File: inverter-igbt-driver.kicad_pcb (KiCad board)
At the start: 2 copper layers, 79 x 32 mm, 41 parts, among them J1 Conn_01x06, U1 NE555, U2 IXDF604SIA, U3 FOD8316, U6 Transformer_2P_2S

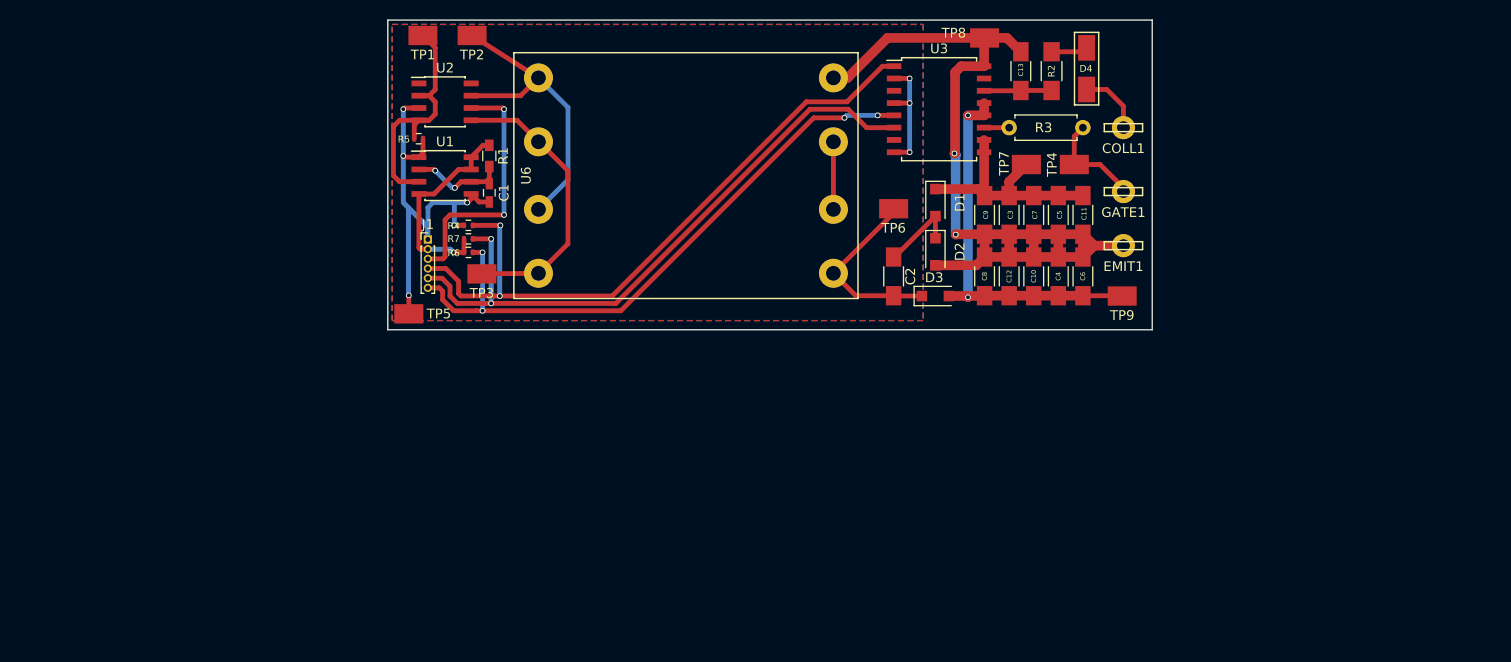
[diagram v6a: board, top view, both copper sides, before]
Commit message: Including both igbt drivers on one board.
WIP
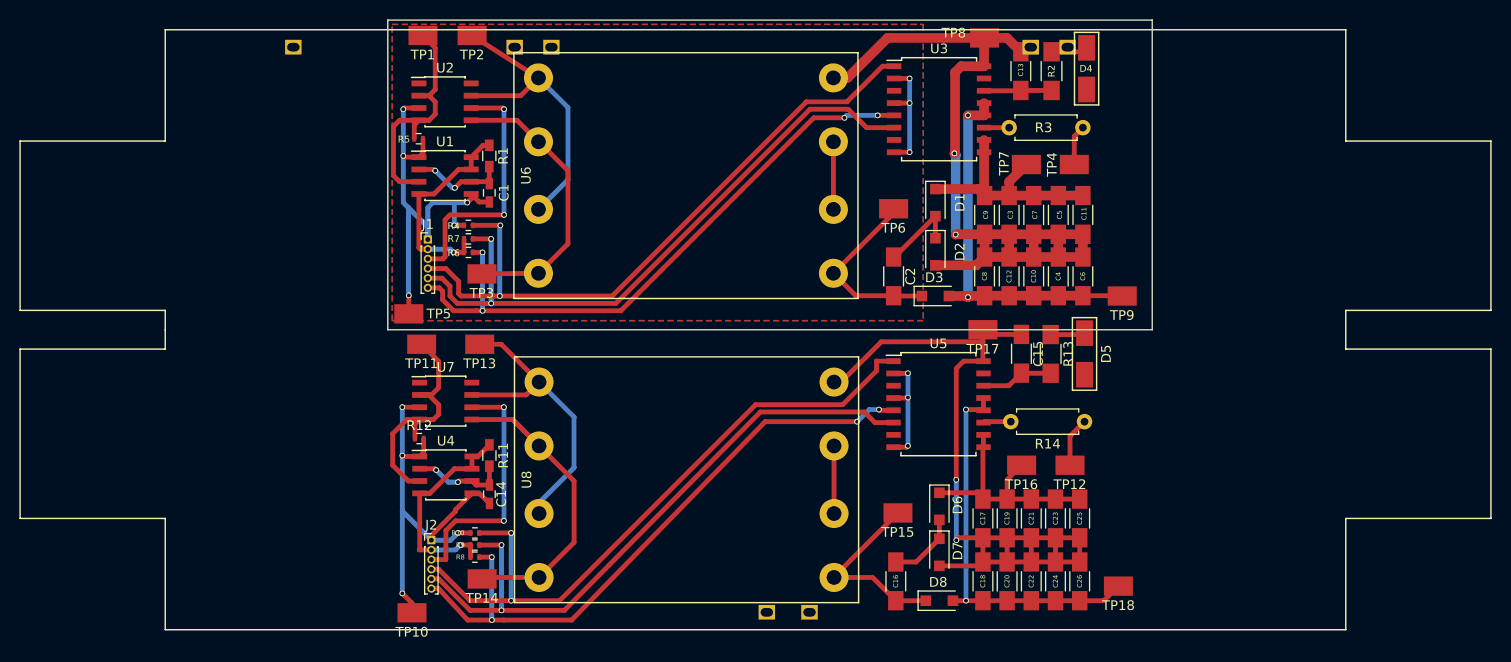
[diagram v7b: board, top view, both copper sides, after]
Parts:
- removed COLL1, EMIT1, GATE1: Conn_01x01, inverter-igbt-driver:CONN_110_TAB
- added C14: 0.01u, Capacitors_SMD:C_0603_HandSoldering, F.Cu at (110.5, 85.0)
- added C15: 100p, Capacitors_SMD:C_1206_HandSoldering, F.Cu at (165.5, 70.5)
- added C16: 10u, Capacitors_SMD:C_1206_HandSoldering, F.Cu at (152.5, 94.0)
- added C17: 10u, Capacitors_SMD:C_1206_HandSoldering, F.Cu at (161.5, 87.5)
- added C18: 10u, Capacitors_SMD:C_1206_HandSoldering, F.Cu at (161.5, 94.0)
- added C19: 10u, Capacitors_SMD:C_1206_HandSoldering, F.Cu at (164.0, 87.5)
- added C20: 10u, Capacitors_SMD:C_1206_HandSoldering, F.Cu at (164.0, 94.0)
- added C21: 10u, Capacitors_SMD:C_1206_HandSoldering, F.Cu at (166.5, 87.5)
- added C22: 10u, Capacitors_SMD:C_1206_HandSoldering, F.Cu at (166.5, 94.0)
- added C23: 10u, Capacitors_SMD:C_1206_HandSoldering, F.Cu at (169.0, 87.5)
- added C24: 10u, Capacitors_SMD:C_1206_HandSoldering, F.Cu at (169.0, 94.0)
- added C25: 10u, Capacitors_SMD:C_1206_HandSoldering, F.Cu at (171.5, 87.5)
- added C26: 10u, Capacitors_SMD:C_1206_HandSoldering, F.Cu at (171.5, 94.0)
- added D5: D, inverter-igbt-driver:DO-214AC, F.Cu at (172.0, 70.5)
- added D6: D_Schottky, Diodes_SMD:D_SOD-123F, F.Cu at (157.0, 86.2)
- added D7: D_Schottky, Diodes_SMD:D_SOD-123F, F.Cu at (157.0, 91.0)
- added D8: D_Schottky, Diodes_SMD:D_SOD-123F, F.Cu at (157.0, 96.0)
- added J2: Conn_01x06, Pin_Headers:Pin_Header_Straight_1x06_Pitch1.00mm, F.Cu at (104.5, 89.8)
- added R10: 1k, Resistors_SMD:R_0402, F.Cu at (109.0, 89.0)
- added R11: 1.5k, Resistors_SMD:R_0603_HandSoldering, F.Cu at (110.5, 81.0)
- added R12: 1k, Resistors_SMD:R_0402, F.Cu at (103.2, 79.2)
- added R13: 100, Resistors_SMD:R_1206_HandSoldering, F.Cu at (168.5, 70.5)
- added R14: 8, Resistors_THT:R_Axial_DIN0207_L6.3mm_D2.5mm_P7.62mm_Horizontal, F.Cu at (172.0, 77.5)
- added R8: 1k, Resistors_SMD:R_0402, F.Cu at (109.0, 91.5)
- added R9: 1k, Resistors_SMD:R_0402, F.Cu at (109.0, 90.2)
- added TP10: TEST, inverter-igbt-driver:TP RCT (0805), F.Cu at (102.5, 97.2)
- added TP11: TEST, inverter-igbt-driver:TP RCT (0805), F.Cu at (103.5, 69.5)
- added TP12: TEST, inverter-igbt-driver:TP RCT (0805), F.Cu at (170.5, 82.0)
- added TP13: TEST, inverter-igbt-driver:TP RCT (0805), F.Cu at (109.5, 69.5)
- added TP14: TEST, inverter-igbt-driver:TP RCT (0805), F.Cu at (109.8, 93.8)
- added TP15: TEST, inverter-igbt-driver:TP RCT (0805), F.Cu at (152.7, 86.9)
- added TP16: TEST, inverter-igbt-driver:TP RCT (0805), F.Cu at (165.5, 82.0)
- added TP17: TEST, inverter-igbt-driver:TP RCT (0805), F.Cu at (161.5, 68.0)
- added TP18: TEST, inverter-igbt-driver:TP RCT (0805), F.Cu at (175.5, 94.5)
- added U4: NE555, Housings_SOIC:SOIC-8_3.9x4.9mm_Pitch1.27mm, F.Cu at (106.0, 83.0)
- added U5: FOD8316, Housings_SOIC:SOIC-16W_7.5x10.3mm_Pitch1.27mm, F.Cu at (156.9, 75.7)
- added U7: IXDF604SIA, Housings_SOIC:SOIC-8_3.9x4.9mm_Pitch1.27mm, F.Cu at (106.0, 75.4)
- added U8: Transformer_2P_2S, inverter-igbt-driver:FS48-050-C2, F.Cu at (130.9, 83.5)
- added U9: IGBT_HALF_BRIDGE, inverter-igbt-driver:MG06600WB-BN4MM, F.Cu at (138.0, 68.0)
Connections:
- net /EMIT renamed /COLL_L
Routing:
- net /EMIT_L: track 0.00 -> 85.5 mm, vias 0 -> 2
- net /VIN_L: track 0.00 -> 70.2 mm, vias 0 -> 2
- net /FAULT_L: track 0.00 -> 67.2 mm, vias 0 -> 2
- net /RESET_L: track 0.00 -> 66.2 mm, vias 0 -> 4
- net GND: track 57.5 -> 114.3 mm, vias 8 -> 15
- net /negative/VDD_IGBT: track 0.00 -> 40.6 mm, vias 0 -> 2
- net Net-(TP14-Pad1): track 0.00 -> 34.0 mm
- net Net-(TP13-Pad1): track 0.00 -> 31.8 mm
- net +24V: track 26.4 -> 52.3 mm, vias 2 -> 4
- net /negative/VSS_IGBT: track 0.00 -> 25.5 mm
- net Net-(R12-Pad1): track 0.00 -> 25.4 mm
- net +5V: track 21.9 -> 44.6 mm, vias 1 -> 2
- net Net-(C16-Pad2): track 0.00 -> 19.9 mm
- net Net-(C14-Pad1): track 0.00 -> 9.94 mm, vias 0 -> 2
- net Net-(C15-Pad2): track 0.00 -> 7.47 mm
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
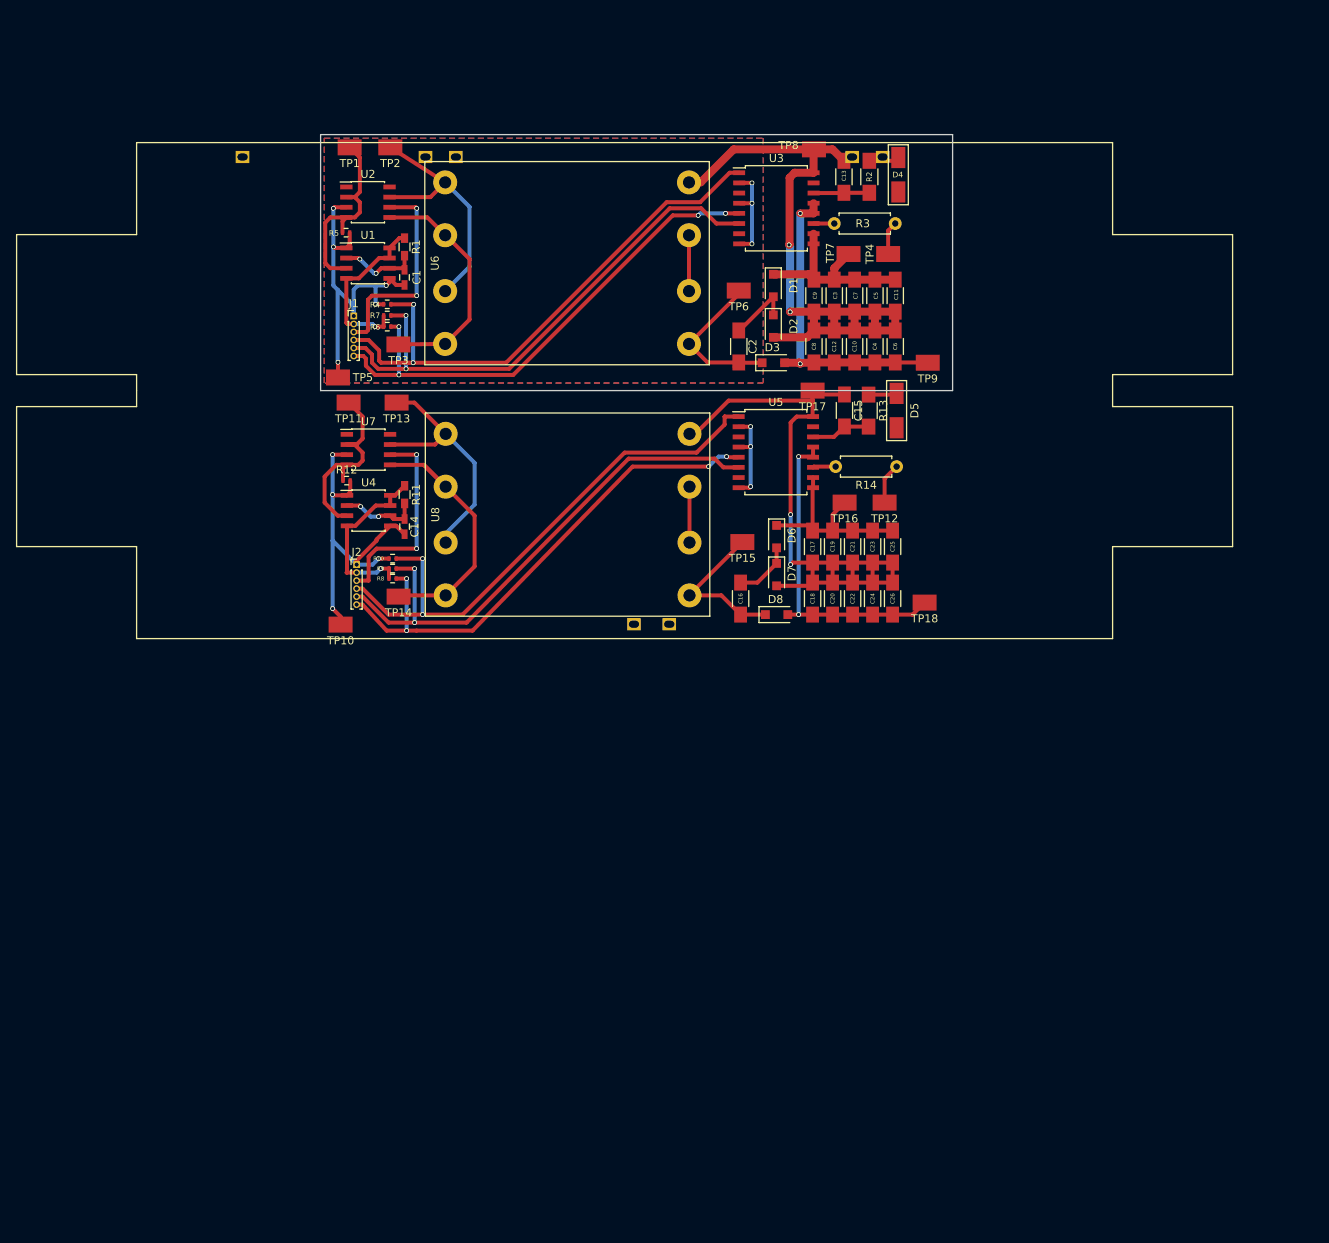
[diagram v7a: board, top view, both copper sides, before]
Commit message: Add _H suffix to hot leg.
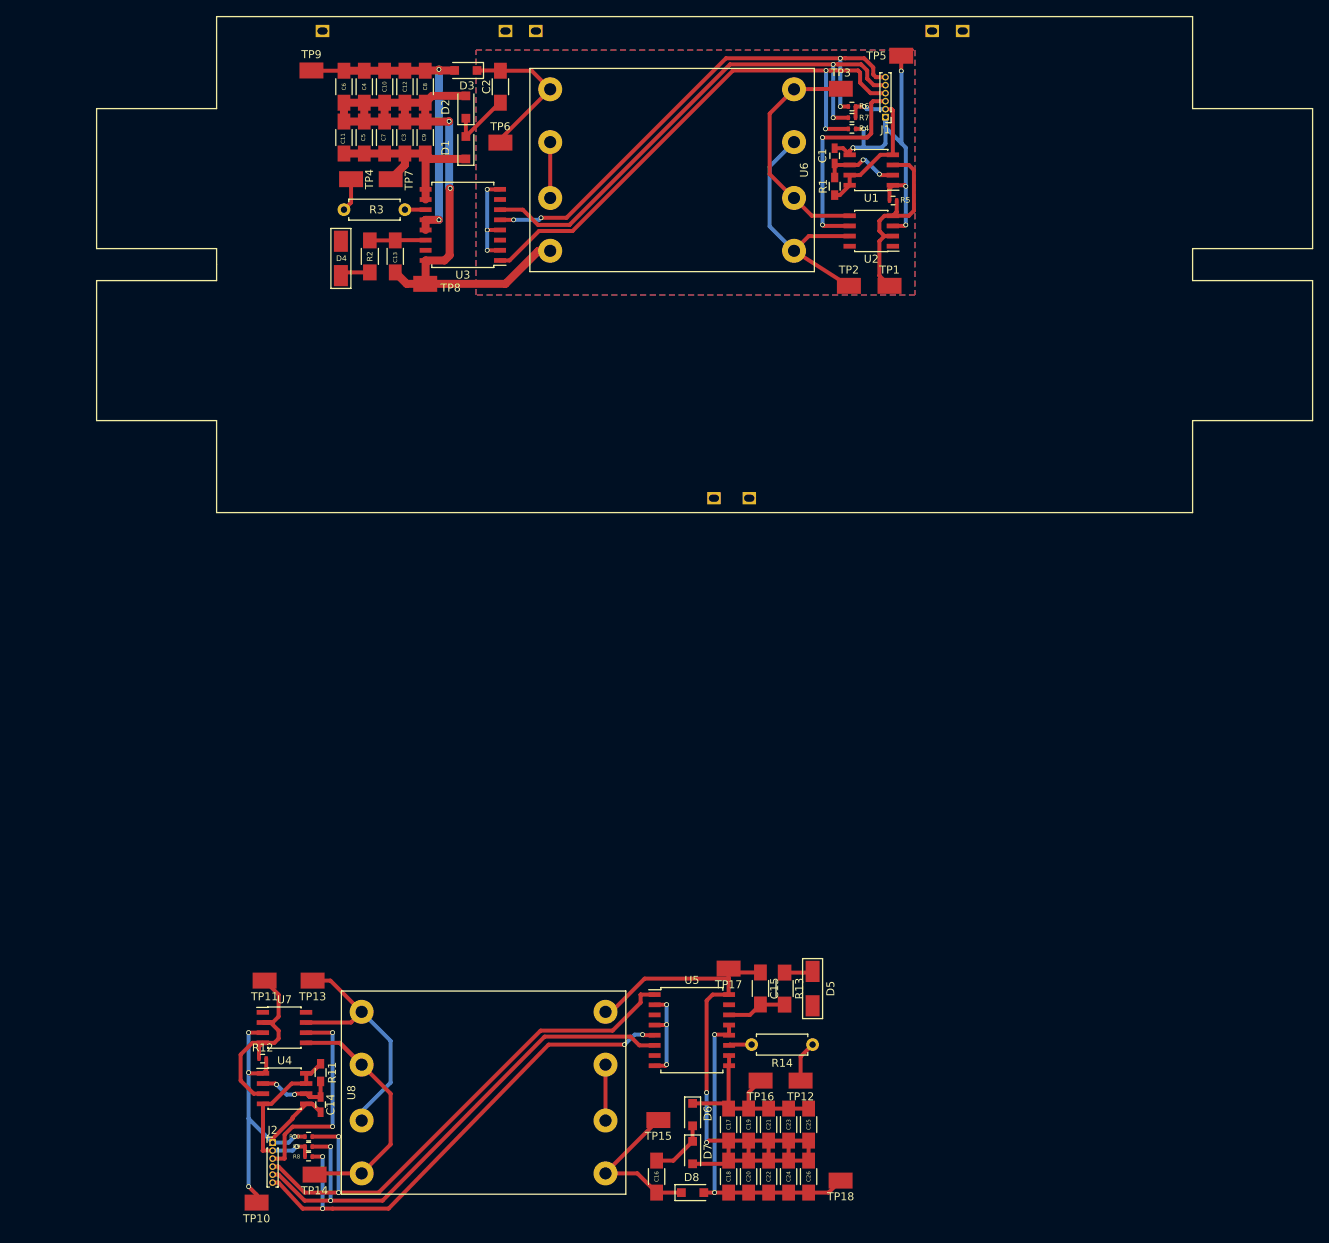
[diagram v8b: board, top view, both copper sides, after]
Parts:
- moved TP9 85.3 mm to (98.9, 28.0), turned to 180 degrees
- moved TP5 81.1 mm to (172.6, 26.1), turned to 180 degrees
- moved C6 76.2 mm to (102.9, 30.0), turned to 90 degrees
- moved C15 73.0 mm to (155.0, 142.7)
- moved U5 73.0 mm to (146.4, 147.9)
- moved U7 73.0 mm to (95.5, 147.6)
- moved C14 73.0 mm to (100.0, 157.2)
- moved C16 73.0 mm to (142.0, 166.2)
- moved C17 73.0 mm to (151.0, 159.8)
- moved C18 73.0 mm to (151.0, 166.2)
- moved C19 73.0 mm to (153.5, 159.8)
- moved C20 73.0 mm to (153.5, 166.2)
- moved C21 73.0 mm to (156.0, 159.8)
- moved C22 73.0 mm to (156.0, 166.2)
- moved C23 73.0 mm to (158.5, 159.8)
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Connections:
- net /COLL renamed /COLL_H
- net /FAULT renamed /FAULT_H
- net /GATE renamed /GATE_H
- net /RESET renamed /RESET_H
- net /VIN renamed /VIN_H
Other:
- board outline removed
